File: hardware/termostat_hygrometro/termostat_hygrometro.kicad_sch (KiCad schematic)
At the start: 5 parts

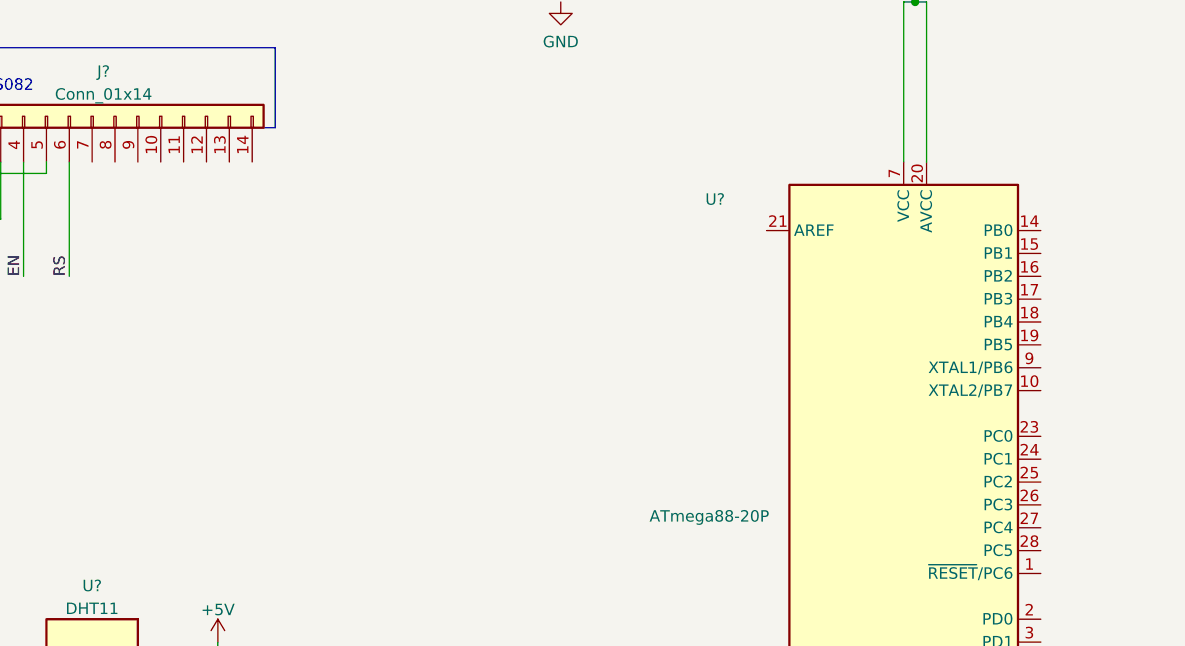
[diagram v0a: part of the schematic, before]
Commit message: hardware - connected the atmega88 pins with lcd and dht11
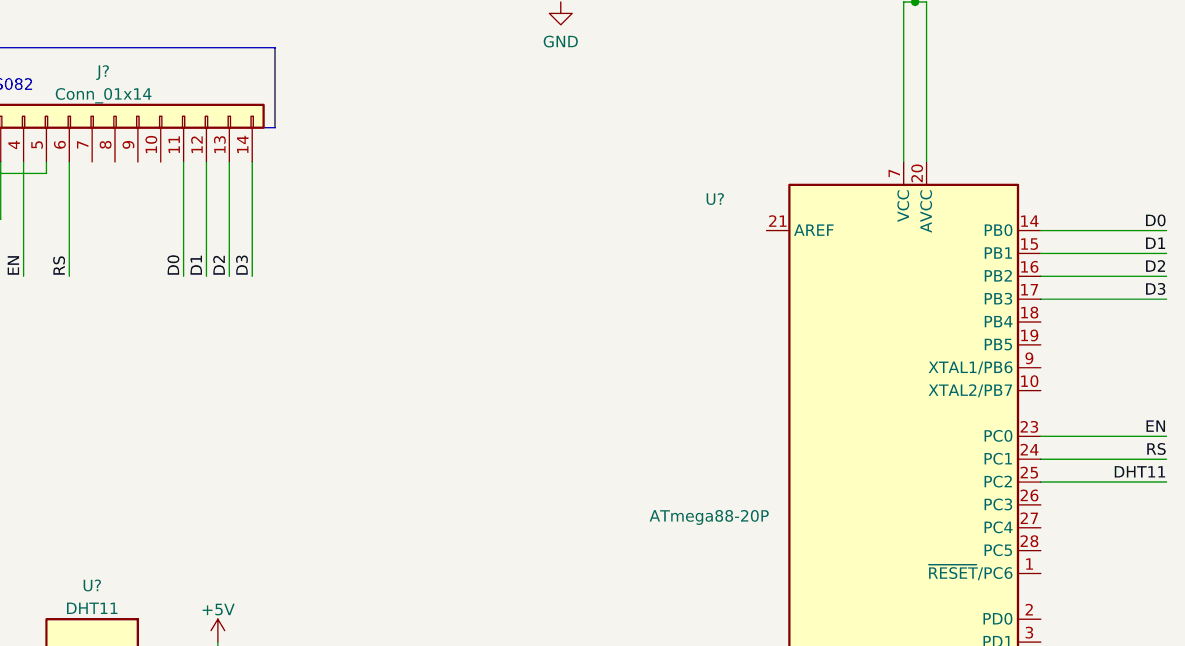
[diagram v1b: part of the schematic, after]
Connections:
- net DHT11: now also U?.25 (PC2)
- net EN: now also U?.23 (PC0)
- net RS: now also U?.24 (PC1)
- net D0: now reaches J?.11 (Pin_11)
- net D0: now also U?.14 (PB0)
- net D1: now reaches J?.12 (Pin_12)
- net D1: now also U?.15 (PB1)
- net D2: now reaches J?.13 (Pin_13)
- net D2: now also U?.16 (PB2)
- net D3: now reaches J?.14 (Pin_14)
- net D3: now also U?.17 (PB3)
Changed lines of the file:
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@@
+    (stroke (width 0) (type default) (color 0 0 0 0))
+  )
+  (wire (pts (xy 247.65 73.66) (xy 261.62 73.66))
     (stroke (width 0) (type default) (color 0 0 0 0))
   )
@@
     (stroke (width 0) (type default) (color 0 0 0 0))
   )
+  (wire (pts (xy 247.65 50.8) (xy 261.62 50.8))
+    (stroke (width 0) (type default) (color 0 0 0 0))
+  )
   (wire (pts (xy 68.58 116.84) (xy 68.58 124.46))
+    (stroke (width 0) (type default) (color 0 0 0 0))
+  )
+  (wire (pts (xy 154.94 43.18) (xy 154.94 55.88))
     (stroke (width 0) (type default) (color 0 0 0 0))
   )
@@
     (stroke (width 0) (type default) (color 0 0 0 0))
   )
+  (wire (pts (xy 247.65 55.88) (xy 261.62 55.88))
+    (stroke (width 0) (type default) (color 0 0 0 0))
+  )
   (wire (pts (xy 139.7 43.18) (xy 139.7 55.88))
     (stroke (width 0) (type default) (color 0 0 0 0))
@@
   )
   (wire (pts (xy 132.08 43.18) (xy 132.08 49.53))
+    (stroke (width 0) (type default) (color 0 0 0 0))
+  )
+  (wire (pts (xy 247.65 53.34) (xy 261.62 53.34))
     (stroke (width 0) (type default) (color 0 0 0 0))
   )
@@
     (stroke (width 0) (type solid) (color 0 0 0 0))
   )
+  (wire (pts (xy 152.4 43.18) (xy 152.4 55.88))
+    (stroke (width 0) (type default) (color 0 0 0 0))
+  )
+  (wire (pts (xy 247.65 76.2) (xy 261.62 76.2))
+    (stroke (width 0) (type default) (color 0 0 0 0))
+  )
+  (wire (pts (xy 247.65 78.74) (xy 261.62 78.74))
+    (stroke (width 0) (type default) (color 0 0 0 0))
+  )
+  (wire (pts (xy 160.02 43.18) (xy 160.02 55.88))
+    (stroke (width 0) (type default) (color 0 0 0 0))
+  )
   (wire (pts (xy 120.65 53.34) (xy 120.65 55.88))
     (stroke (width 0) (type default) (color 0 0 0 0))
@@
     (stroke (width 0) (type default) (color 0 0 0 0))
   )
+  (wire (pts (xy 247.65 58.42) (xy 261.62 58.42))
+    (stroke (width 0) (type default) (color 0 0 0 0))
+  )
   (wire (pts (xy 234.95 43.18) (xy 234.95 25.4))
     (stroke (width 0) (type default) (color 0 0 0 0))
@@
     (stroke (width 0) (type default) (color 0 0 0 0))
   )
+  (wire (pts (xy 157.48 43.18) (xy 157.48 55.88))
+    (stroke (width 0) (type default) (color 0 0 0 0))
+  )
   (text "LCD 2x8\nEA DISPS082" (at 124.46 35.56 0)
+    (effects (font (size 1.27 1.27)) (justify left bottom))
+  )
+  (label "D2" (at 157.48 55.88 90)
     (effects (font (size 1.27 1.27)) (justify left bottom))
   )
@@
     (effects (font (size 1.27 1.27)) (justify left bottom))
   )
+  (label "D0" (at 152.4 55.88 90)
+    (effects (font (size 1.27 1.27)) (justify left bottom))
+  )
+  (label "RS" (at 261.62 76.2 180)
+    (effects (font (size 1.27 1.27)) (justify right bottom))
+  )
+  (label "D3" (at 160.02 55.88 90)
+    (effects (font (size 1.27 1.27)) (justify left bottom))
+  )
   (label "DHT11" (at 156.21 115.57 180)
+    (effects (font (size 1.27 1.27)) (justify right bottom))
+  )
+  (label "D0" (at 261.62 50.8 180)
+    (effects (font (size 1.27 1.27)) (justify right bottom))
+  )
+  (label "D3" (at 261.62 58.42 180)
+    (effects (font (size 1.27 1.27)) (justify right bottom))
+  )
+  (label "EN" (at 261.62 73.66 180)
+    (effects (font (size 1.27 1.27)) (justify right bottom))
+  )
+  (label "D1" (at 154.94 55.88 90)
+    (effects (font (size 1.27 1.27)) (justify left bottom))
+  )
+  (label "DHT11" (at 261.62 78.74 180)
     (effects (font (size 1.27 1.27)) (justify right bottom))
   )
@@
     (effects (font (size 1.27 1.27)) (justify left bottom))
   )
+  (label "D1" (at 261.62 53.34 180)
+    (effects (font (size 1.27 1.27)) (justify right bottom))
+  )
+  (label "D2" (at 261.62 55.88 180)
+    (effects (font (size 1.27 1.27)) (justify right bottom))
+  )
   (symbol (lib_id "power:+5V") (at 156.21 96.52 0) (unit 1)

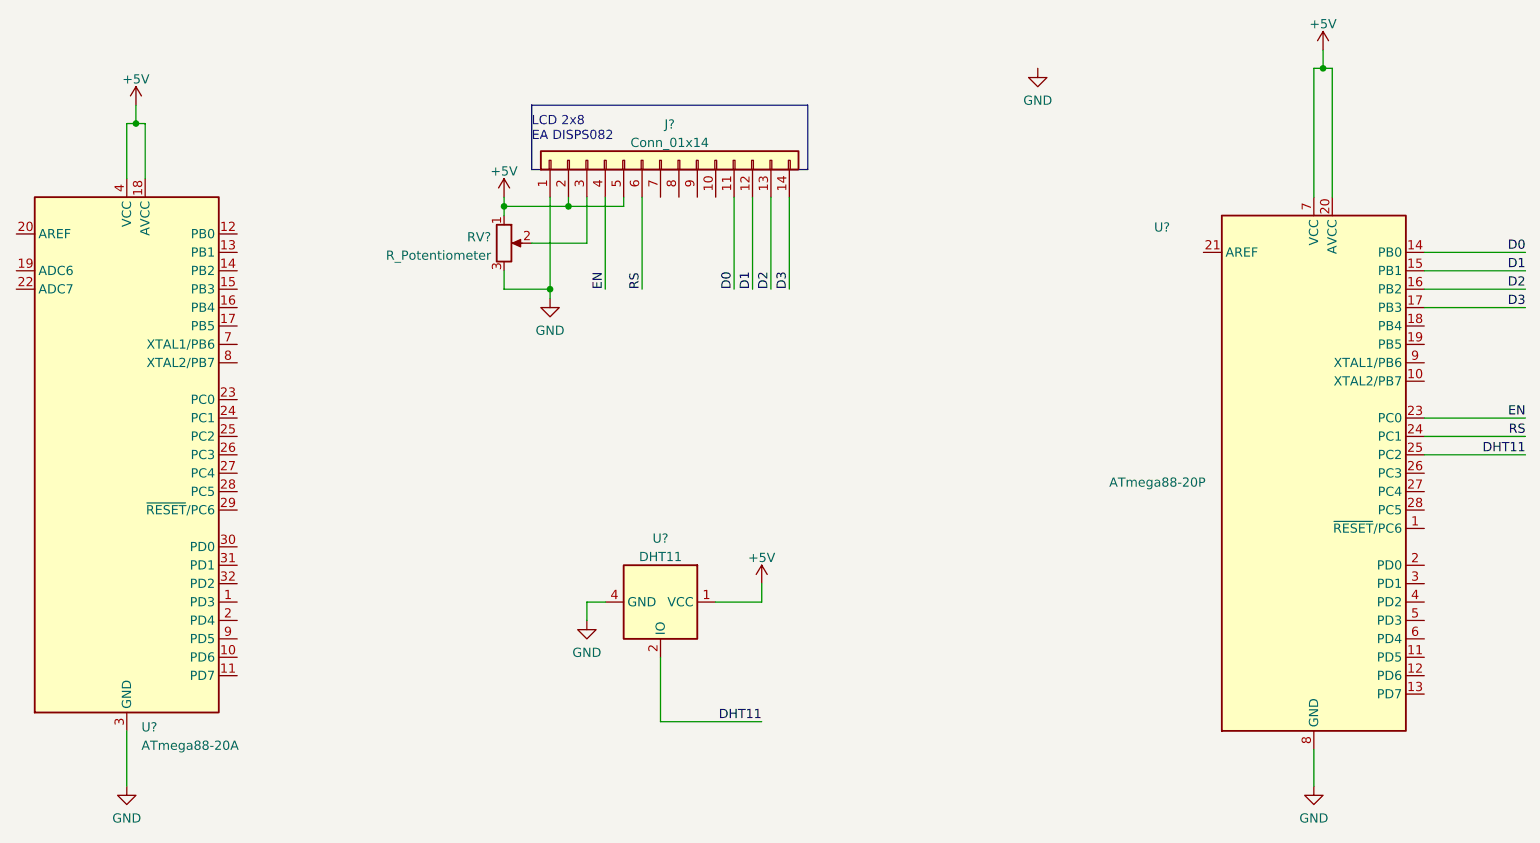
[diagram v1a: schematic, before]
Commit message: modified the pins of the LCD and pin of the DHT11, and added the resisitor to the DHT11 output.
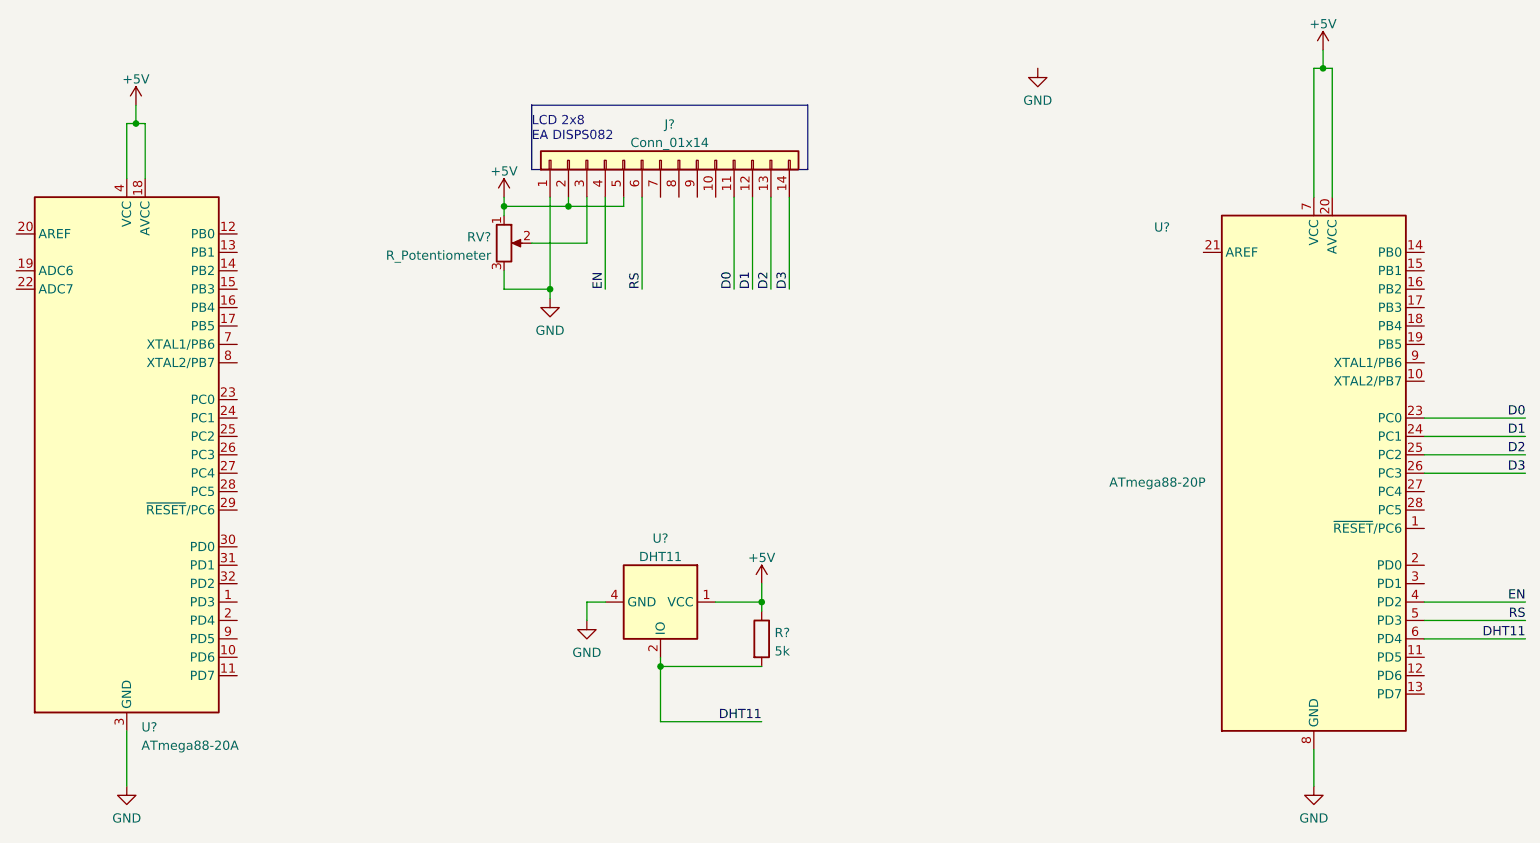
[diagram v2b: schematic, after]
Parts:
- added R?: 5k, symbol Device:R
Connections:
- net +5V: now also R?.1
- net D0: now also U?.23 (PC0); no longer U?.14 (PB0)
- net D1: now also U?.24 (PC1); no longer U?.15 (PB1)
- net D2: now also U?.25 (PC2); no longer U?.16 (PB2)
- net D3: now also U?.26 (PC3); no longer U?.17 (PB3)
- net DHT11: now also U?.6 (PD4), R?.2; no longer U?.25 (PC2)
- net EN: now also U?.4 (PD2); no longer U?.23 (PC0)
- net RS: now also U?.5 (PD3); no longer U?.24 (PC1)
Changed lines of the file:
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@@
 (kicad_sch (version 20211123) (generator eeschema)
   (paper "A4")
+  (junction (at 142.24 107.95) (diameter 0) (color 0 0 0 0)
+  )
   (junction (at 233.68 25.4) (diameter 0) (color 0 0 0 0)
   )
@@
   (junction (at 127 55.88) (diameter 0) (color 0 0 0 0)
   )
+  (junction (at 156.21 99.06) (diameter 0) (color 0 0 0 0)
+  )
   (junction (at 69.85 33.02) (diameter 0) (color 0 0 0 0)
   )
@@
     (stroke (width 0) (type default) (color 0 0 0 0))
   )
+  (wire (pts (xy 69.85 30.48) (xy 69.85 33.02))
+    (stroke (width 0) (type default) (color 0 0 0 0))
+  )
+  (wire (pts (xy 156.21 96.52) (xy 156.21 99.06))
+    (stroke (width 0) (type default) (color 0 0 0 0))
+  )
+  (wire (pts (xy 233.68 22.86) (xy 233.68 25.4))
+    (stroke (width 0) (type default) (color 0 0 0 0))
+  )
+  (wire (pts (xy 68.58 40.64) (xy 68.58 33.02))
+    (stroke (width 0) (type default) (color 0 0 0 0))
+  )
   (wire (pts (xy 247.65 73.66) (xy 261.62 73.66))
     (stroke (width 0) (type default) (color 0 0 0 0))
   )
-  (wire (pts (xy 69.85 30.48) (xy 69.85 33.02))
-    (stroke (width 0) (type default) (color 0 0 0 0))
-  )
-  (wire (pts (xy 156.21 96.52) (xy 156.21 99.06))
-    (stroke (width 0) (type default) (color 0 0 0 0))
-  )
-  (wire (pts (xy 233.68 22.86) (xy 233.68 25.4))
-    (stroke (width 0) (type default) (color 0 0 0 0))
-  )
-  (wire (pts (xy 68.58 40.64) (xy 68.58 33.02))
-    (stroke (width 0) (type default) (color 0 0 0 0))
-  )
-  (wire (pts (xy 247.65 50.8) (xy 261.62 50.8))
+  (wire (pts (xy 156.21 99.06) (xy 156.21 100.33))
     (stroke (width 0) (type default) (color 0 0 0 0))
   )
@@
     (stroke (width 0) (type default) (color 0 0 0 0))
   )
-  (wire (pts (xy 247.65 55.88) (xy 261.62 55.88))
-    (stroke (width 0) (type default) (color 0 0 0 0))
-  )
   (wire (pts (xy 139.7 43.18) (xy 139.7 55.88))
     (stroke (width 0) (type default) (color 0 0 0 0))
@@
     (stroke (width 0) (type default) (color 0 0 0 0))
   )
+  (wire (pts (xy 247.65 104.14) (xy 261.62 104.14))
+    (stroke (width 0) (type default) (color 0 0 0 0))
+  )
   (wire (pts (xy 134.62 99.06) (xy 132.08 99.06))
     (stroke (width 0) (type default) (color 0 0 0 0))
@@
     (stroke (width 0) (type default) (color 0 0 0 0))
   )
-  (wire (pts (xy 247.65 53.34) (xy 261.62 53.34))
-    (stroke (width 0) (type default) (color 0 0 0 0))
-  )
   (wire (pts (xy 120.65 44.45) (xy 129.54 44.45))
     (stroke (width 0) (type default) (color 0 0 0 0))
   )
+  (wire (pts (xy 247.65 99.06) (xy 261.62 99.06))
+    (stroke (width 0) (type default) (color 0 0 0 0))
+  )
   (wire (pts (xy 233.68 25.4) (xy 234.95 25.4))
+    (stroke (width 0) (type default) (color 0 0 0 0))
+  )
+  (wire (pts (xy 247.65 101.6) (xy 261.62 101.6))
     (stroke (width 0) (type default) (color 0 0 0 0))
   )
@@
     (stroke (width 0) (type default) (color 0 0 0 0))
   )
+  (wire (pts (xy 247.65 78.74) (xy 261.62 78.74))
+    (stroke (width 0) (type default) (color 0 0 0 0))
+  )
+  (wire (pts (xy 142.24 107.95) (xy 156.21 107.95))
+    (stroke (width 0) (type default) (color 0 0 0 0))
+  )
   (wire (pts (xy 247.65 76.2) (xy 261.62 76.2))
     (stroke (width 0) (type default) (color 0 0 0 0))
   )
-  (wire (pts (xy 247.65 78.74) (xy 261.62 78.74))
+  (wire (pts (xy 142.24 107.95) (xy 142.24 115.57))
+    (stroke (width 0) (type default) (color 0 0 0 0))
+  )
+  (wire (pts (xy 247.65 81.28) (xy 261.62 81.28))
     (stroke (width 0) (type default) (color 0 0 0 0))
   )
@@
     (stroke (width 0) (type default) (color 0 0 0 0))
   )
-  (wire (pts (xy 142.24 106.68) (xy 142.24 115.57))
+  (wire (pts (xy 142.24 106.68) (xy 142.24 107.95))
     (stroke (width 0) (type default) (color 0 0 0 0))
   )
@@
     (stroke (width 0) (type default) (color 0 0 0 0))
   )
-  (wire (pts (xy 247.65 58.42) (xy 261.62 58.42))
-    (stroke (width 0) (type default) (color 0 0 0 0))
-  )
   (wire (pts (xy 234.95 43.18) (xy 234.95 25.4))
     (stroke (width 0) (type default) (color 0 0 0 0))
@@
     (effects (font (size 1.27 1.27)) (justify left bottom))
   )
+  (label "DHT11" (at 261.62 104.14 180)
+    (effects (font (size 1.27 1.27)) (justify right bottom))
+  )
   (label "D0" (at 152.4 55.88 90)
     (effects (font (size 1.27 1.27)) (justify left bottom))
   )
-  (label "RS" (at 261.62 76.2 180)
+  (label "EN" (at 261.62 99.06 180)
+    (effects (font (size 1.27 1.27)) (justify right bottom))
+  )
+  (label "D0" (at 261.62 73.66 180)
+    (effects (font (size 1.27 1.27)) (justify right bottom))
+  )
+  (label "D2" (at 261.62 78.74 180)
     (effects (font (size 1.27 1.27)) (justify right bottom))
   )
@@
     (effects (font (size 1.27 1.27)) (justify left bottom))
   )
+  (label "D1" (at 261.62 76.2 180)
+    (effects (font (size 1.27 1.27)) (justify right bottom))
+  )
+  (label "D3" (at 261.62 81.28 180)
+    (effects (font (size 1.27 1.27)) (justify right bottom))
+  )
   (label "DHT11" (at 156.21 115.57 180)
     (effects (font (size 1.27 1.27)) (justify right bottom))
   )
-  (label "D0" (at 261.62 50.8 180)
-    (effects (font (size 1.27 1.27)) (justify right bottom))
-  )
-  (label "D3" (at 261.62 58.42 180)
-    (effects (font (size 1.27 1.27)) (justify right bottom))
-  )
-  (label "EN" (at 261.62 73.66 180)
+  (label "RS" (at 261.62 101.6 180)
     (effects (font (size 1.27 1.27)) (justify right bottom))
   )
@@
     (effects (font (size 1.27 1.27)) (justify left bottom))
   )
-  (label "DHT11" (at 261.62 78.74 180)
-    (effects (font (size 1.27 1.27)) (justify right bottom))
-  )
   (label "EN" (at 134.62 55.88 90)
     (effects (font (size 1.27 1.27)) (justify left bottom))
-  )
-  (label "D1" (at 261.62 53.34 180)
-    (effects (font (size 1.27 1.27)) (justify right bottom))
-  )
-  (label "D2" (at 261.62 55.88 180)
-    (effects (font (size 1.27 1.27)) (justify right bottom))
   )
   (symbol (lib_id "power:+5V") (at 156.21 96.52 0) (unit 1)
@@
     (pin "4")
   )
+  (symbol (lib_id "Device:R") (at 156.21 104.14 0) (unit 1)
+    (in_bom yes) (on_board yes) (fields_autoplaced)
+    (property "Reference" "R?" (id 0) (at 157.988 103.3053 0)
+      (effects (font (size 1.27 1.27)) (justify left))
+    )
+    (property "Value" "5k" (id 1) (at 157.988 105.8422 0)
+      (effects (font (size 1.27 1.27)) (justify left))
+    )
+    (property "Footprint" "" (id 2) (at 154.432 104.14 90)
+      (effects (font (size 1.27 1.27)) hide)
+    )
+    (property "Datasheet" "~" (id 3) (at 156.21 104.14 0)
+      (effects (font (size 1.27 1.27)) hide)
+    )
+    (pin "1")
+    (pin "2")
+  )
   (symbol (lib_id "power:+5V") (at 69.85 30.48 0) (unit 1)
     (in_bom yes) (on_board yes)
@@
       (reference "J?") (unit 1) (value "Conn_01x14") (footprint "")
     )
+    (path "/c7b2ddf0-3c09-49f4-9a99-92a380162a4e"
+      (reference "R?") (unit 1) (value "5k") (footprint "")
+    )
     (path "/e8aaf0c3-ffe6-43a6-92a0-ebaf0ba8840a"
